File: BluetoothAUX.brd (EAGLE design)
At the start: 39.4 x 39.4 mm, 29 parts, among them IC1 NE5532D, X2 MINI-USB-SCHIELD-32005-201, X3 STEREOJACK

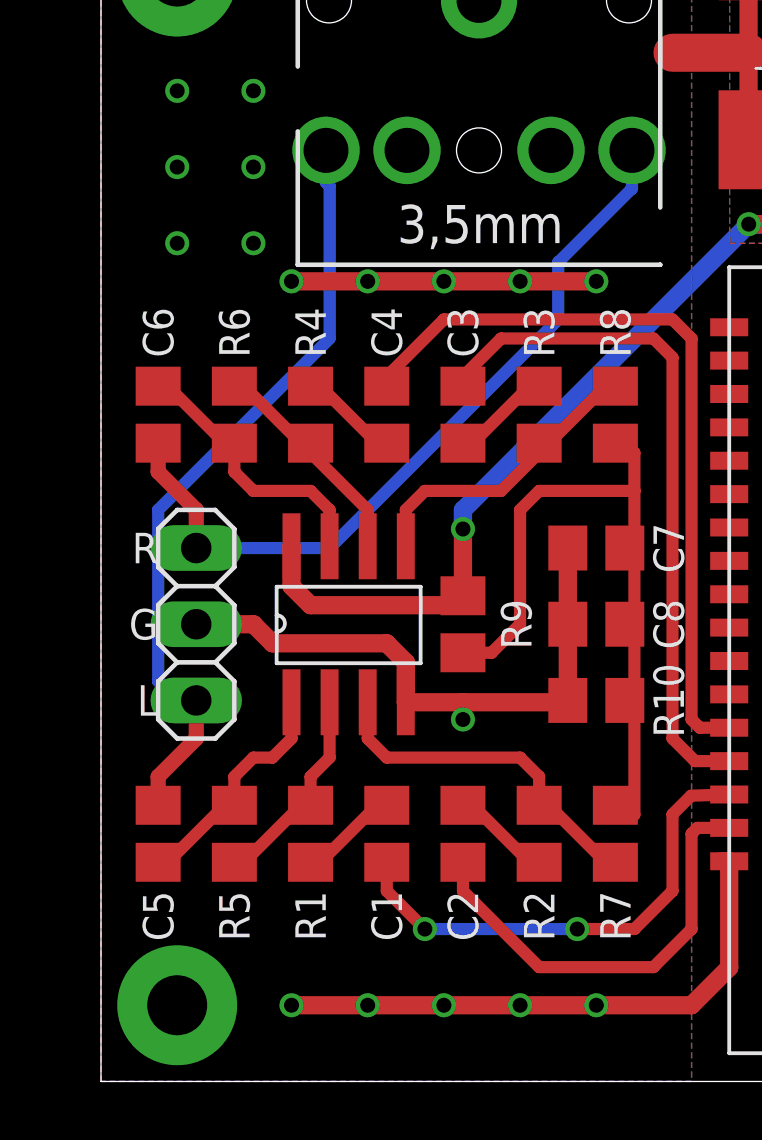
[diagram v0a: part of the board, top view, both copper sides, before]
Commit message: Add trimmers
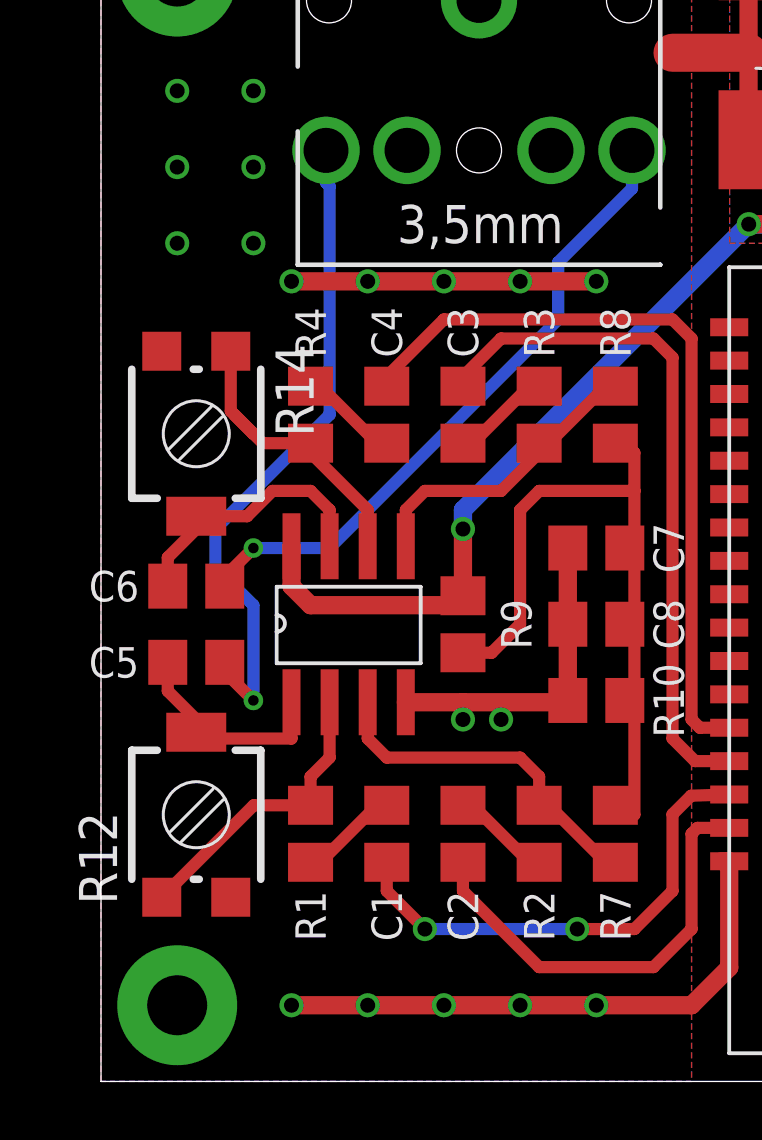
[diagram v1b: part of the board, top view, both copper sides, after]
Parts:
- removed JP9: SPEAKER, pinhead:1X03
- removed R5, R6: 10K, rcl:R0805
- added R12, R14: (no value), resistor:RTRIM3314G
- moved C6 5.85 mm to (48.9, 31.8), turned to 0 degrees
- moved C5 5.85 mm to (48.9, 29.2), turned to 0 degrees
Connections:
- net GND: no longer JP9.2
- net N$1: now also R12.3; no longer R5.1
- net N$10: now also R14.2; no longer R6.2
- net N$3: now also R14.3; no longer R6.1
- net N$9: now also R12.2; no longer R5.2
- net SPK_L: no longer JP9.1
- net SPK_R: no longer JP9.3
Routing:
- net GND: track 94.7 -> 85.9 mm, vias 23 -> 24
- net SPK_R: track 25.9 -> 21.6 mm, vias 0 -> 1
- net SPK_L: track 25.7 -> 22.2 mm, vias 0 -> 1
- net N$1: track 7.35 -> 10.2 mm
- net N$3: track 7.91 -> 10.5 mm
- net N$9: track 7.92 -> 7.28 mm
- net N$10: track 9.55 -> 8.99 mm
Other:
- board text removed: "G"
- board text removed: "L"
- board text removed: "R"

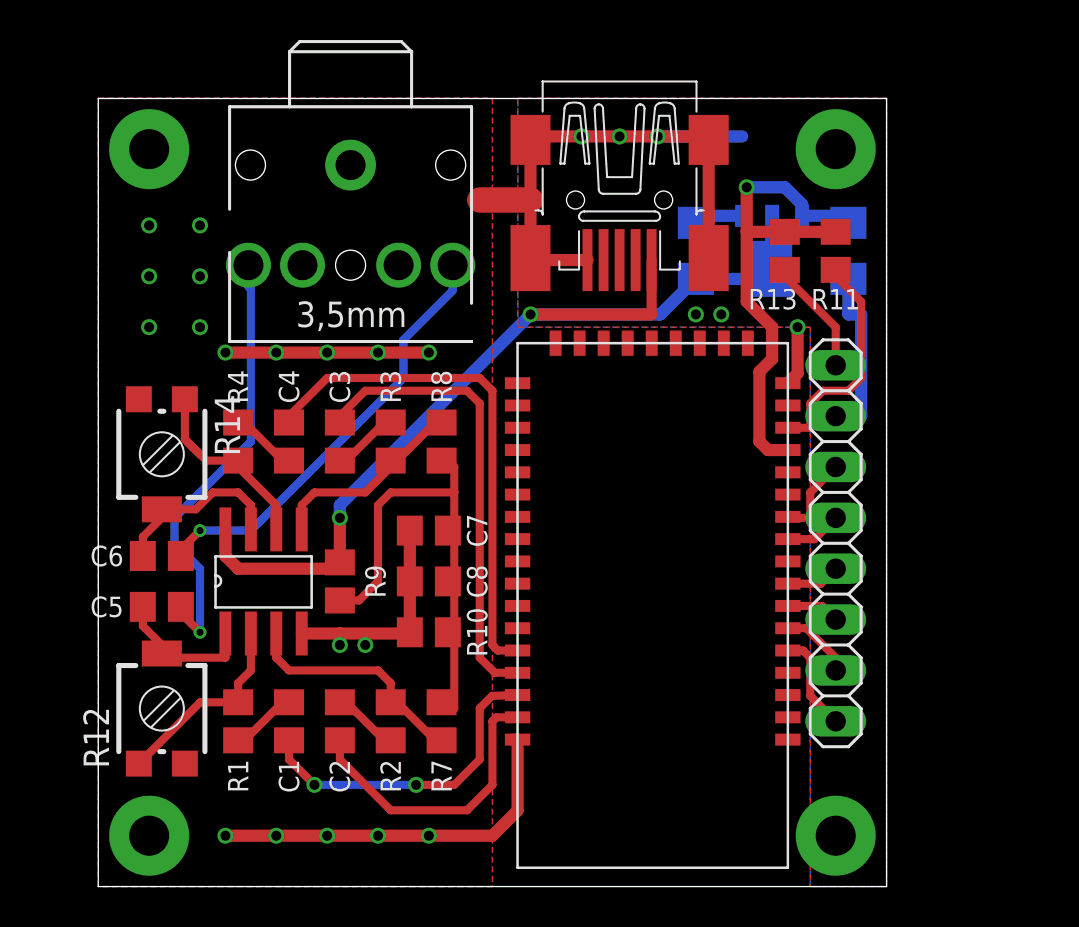
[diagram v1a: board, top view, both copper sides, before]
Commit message: Drop DCDC for direct USB supply
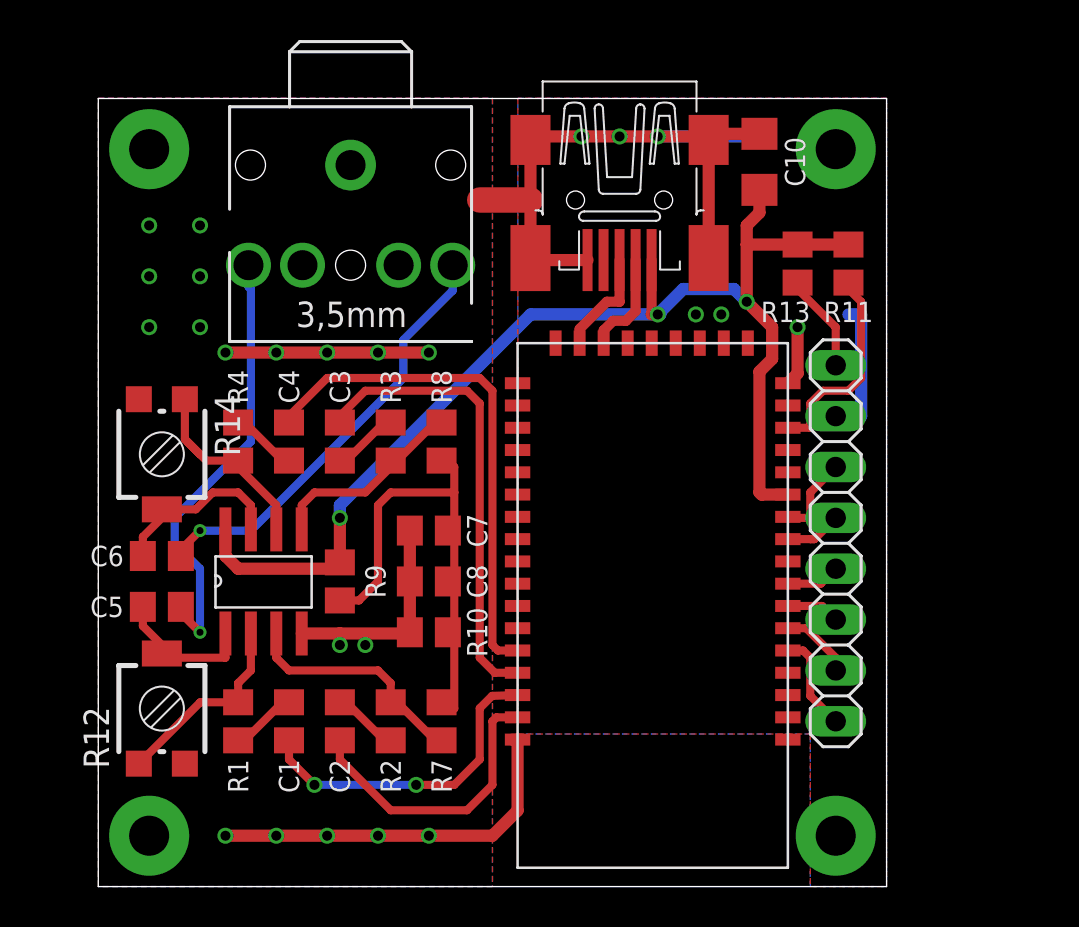
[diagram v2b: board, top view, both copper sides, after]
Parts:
- removed C12: 10uF, rcl:C1206
- removed HT7536: 7536, BT:SOT89R
- moved C10 5.46 mm to (78.7, 51.4), flipped to the top
- moved R11 0.90 mm to (83.2, 46.4)
- moved R13 0.90 mm to (80.6, 46.4)
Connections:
- removed net +3V3: C12.1, HT7536.1, R11.1, R13.2, U$1.P$14
- removed net VBUS: U$1.P$12
- new net BAT: U$1.P$14
- new net N$18: U$1.P$24, X2.2
- new net N$19: U$1.P$25, X2.3
- net +5V: now also R11.1, R13.2, U$1.P$12; no longer HT7536.3, HT7536.4
- net GND: no longer C12.2, HT7536.2
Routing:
- net +3V3: track 25.7 -> 0.00 mm, vias 1 -> 0
- net +5V: track 51.0 -> 62.0 mm, vias 2 -> 3
- net N$19: track 0.00 -> 5.35 mm
- net N$18: track 0.00 -> 5.18 mm
- net GND: track 85.9 -> 84.2 mm
- net N$13: track 11.4 -> 10.5 mm
- net COM: track 5.82 -> 4.92 mm

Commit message: TPA6132A
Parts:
- removed C10: 10uF, rcl:C1206
- removed C6: 1uF, rcl:C0805
- removed C7: 4.7uF, rcl:C0805
- removed C8: 10nF, rcl:C0805
- removed IC1: NE5532D, BT:SO08
- removed R10, R9: 100K, rcl:R0805
- removed R11, R13, R4, R7, R8: 10K, rcl:R0805
- removed R12, R14: (no value), resistor:RTRIM3314G
- removed X3: STEREOJACK, adafruit:STX3100
- added IC2: TPA6132A2, texas:QFN16
- added RN1: CTS742C083, resistor-net:CTS742C083
- added X1: STEREOJACK, adafruit:STX3100
- C1, C3: device rcl:C0805 -> resistor:C0603
- C2, C4: value 1uF -> 2.2uF; device rcl:C0805 -> resistor:C0603
- C5: value 1uF -> 10uF; device rcl:C0805 -> rcl:C1206
- R1: device rcl:R0805 -> resistor:R0603
- R2, R3: value 10K -> (none); device rcl:R0805 -> resistor:R0603
- moved X2 24.5 mm to (50.8, 36.8), turned to 0 degrees
- moved C4 21.9 mm to (64.8, 17.8)
- moved C5 15.8 mm to (59.1, 41.3)
- moved C3 11.2 mm to (59.1, 26.4), turned to 90 degrees
- moved R1 11.1 mm to (62.2, 17.8)
- moved C1 8.28 mm to (59.7, 30.5)
- moved R3 8.28 mm to (64.8, 30.5), turned to 90 degrees
- moved R2 7.24 mm to (62.2, 30.5)
- moved C2 6.02 mm to (59.7, 17.8), turned to 270 degrees
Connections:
- removed net N$1: IC1.2, R1.2, R12.3
- removed net N$10: C6.1, IC1.7, R14.2
- removed net N$11: C7.1, C8.1, R10.2, R7.1, R8.2, R9.1
- removed net N$2: IC1.3, R2.2, R7.2
- removed net N$3: IC1.6, R14.3, R4.2
- removed net N$4: IC1.5, R3.2, R8.1
- removed net N$5: C1.2, R1.1
- removed net N$6: C2.2, R2.1
- removed net N$7: C3.2, R3.1
- removed net N$8: C4.2, R4.1
- removed net N$9: C5.1, IC1.1, R12.2
- removed net SPK_L: C5.2, X3.5
- removed net SPK_R: C6.2, X3.2
- new net N$14: IC2.5, X1.2
- new net N$20: IC2.16, X1.5
- new net N$26: C3.1, IC2.11
- new net N$27: C3.2, IC2.9
- new net N$28: C1.1, IC2.8
- new net N$29: C2.1, IC2.12
- new net N$30: IC2.13, R1.1
- new net N$31: IC2.6, R3.2, RN1.6
- new net N$32: IC2.7, R2.2, RN1.5
- new net SGND: IC2.15, X1.1
- net +5V: now also C4.1, C5.1, IC2.14, R1.2, RN1.1, RN1.2, RN1.3, RN1.4; no longer C10.1, IC1.8, R11.1, R13.2, R9.2
- net COM: now also RN1.8; no longer R13.1
- net GND: now also C1.2, C2.2, C4.2, C5.2, IC2.10, R2.1, R3.1; no longer C10.2, C7.2, C8.2, IC1.4, R10.1, X3.1
- net N$13: now also RN1.7; no longer R11.2
- net SPK_LN: now also IC2.1; no longer C1.1
- net SPK_LP: now also IC2.2; no longer C2.1
- net SPK_RN: now also IC2.4; no longer C4.1
- net SPK_RP: now also IC2.3; no longer C3.1
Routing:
- net GND: track 84.2 -> 19.9 mm, vias 24 -> 17
- net SGND: track 0.00 -> 24.8 mm, vias 0 -> 1
- net N$11: track 24.7 -> 0.00 mm
- net SPK_L: track 22.2 -> 0.00 mm, vias 1 -> 0
- net SPK_R: track 21.6 -> 0.00 mm, vias 1 -> 0
- net SPK_RN: track 25.6 -> 5.12 mm
- net SPK_RP: track 23.0 -> 4.87 mm
- net COM: track 4.92 -> 21.9 mm, vias 0 -> 1
- net N$18: track 5.18 -> 20.1 mm, vias 0 -> 2
- net N$19: track 5.35 -> 20.2 mm
- net N$20: track 0.00 -> 13.4 mm, vias 0 -> 1
- net N$31: track 0.00 -> 11.9 mm
- net N$2: track 11.7 -> 0.00 mm
- net N$14: track 0.00 -> 11.0 mm, vias 0 -> 1
- net SPK_LP: track 14.7 -> 3.78 mm
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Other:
- board size 39.4 x 39.4 mm -> 38.7 x 28.6 mm

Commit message: LEDs
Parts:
- added LED1, LED2: (no value), led:LED3MM
- added RN2: 1K, resistor-net:CTS742C083
- RN1: value CTS742C083 -> 10K
- moved C5 9.09 mm to (57.1, 32.4), turned to 270 degrees
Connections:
- new net LED1+: LED1.K, U$1.P$3
- new net LED1-: LED1.A, RN2.7
- new net LED2+: LED2.K, U$1.P$2
- new net LED2-: LED2.A, RN2.8
- net GND: now also RN2.1, RN2.2, RN2.3, RN2.4
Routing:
- net LED2+: track 0.00 -> 31.4 mm, vias 0 -> 1
- net LED1+: track 0.00 -> 25.7 mm
- net GND: track 19.9 -> 26.7 mm, vias 17 -> 16
- net LED2-: track 0.00 -> 5.36 mm
- net LED1-: track 0.00 -> 3.18 mm
- net N$19: track 20.2 -> 22.8 mm, vias 0 -> 2
- net +5V: track 61.1 -> 62.6 mm
- net N$18: track 20.1 -> 21.3 mm

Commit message: Proper RN symbols
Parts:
- RN1, RN2: device resistor-net:CTS742C083 -> resistor-dil:0603-ARC
- turned RN1 to 90 degrees
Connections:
- net +5V: now also RN1.5, RN1.6, RN1.7, RN1.8; no longer RN1.1, RN1.2, RN1.3, RN1.4
- net COM: now also RN1.4; no longer RN1.8
- net N$13: now also RN1.3; no longer RN1.7
- net N$31: now also RN1.2; no longer RN1.6
- net N$32: now also RN1.1; no longer RN1.5
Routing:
- net GND: track 26.7 -> 23.9 mm
- net +5V: track 62.6 -> 64.1 mm
